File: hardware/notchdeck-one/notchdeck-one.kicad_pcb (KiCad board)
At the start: 4 copper layers, 0 parts

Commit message: Add verified provisional controller PCB floorplan
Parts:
- added C1: 100nF, Capacitor_SMD:C_0402_1005Metric, F.Cu at (92.5, 68.5)
- added C10: 100nF, Capacitor_SMD:C_0402_1005Metric, F.Cu at (61.5, 83.0)
- added C11: 100nF, Capacitor_SMD:C_0402_1005Metric, F.Cu at (75.7, 111.5)
- added C12: 1uF, Capacitor_SMD:C_0402_1005Metric, F.Cu at (75.7, 114.0)
- added C13: 1uF, Capacitor_SMD:C_0805_2012Metric, F.Cu at (119.0, 72.0)
- added C14: 100nF, Capacitor_SMD:C_0402_1005Metric, F.Cu at (66.5, 99.5)
- added C15: 100nF, Capacitor_SMD:C_0402_1005Metric, F.Cu at (66.5, 111.5)
- added C16: 100nF, Capacitor_SMD:C_0402_1005Metric, F.Cu at (66.5, 123.5)
- added C17: 100nF, Capacitor_SMD:C_0402_1005Metric, F.Cu at (66.5, 135.5)
- added C18: 4.7uF, Capacitor_SMD:C_0805_2012Metric, F.Cu at (69.5, 73.0)
- added C19: 4.7uF, Capacitor_SMD:C_0805_2012Metric, F.Cu at (62.5, 74.0)
- added C2: 100nF, Capacitor_SMD:C_0402_1005Metric, F.Cu at (97.2, 68.5)
- added C20: 100nF, Capacitor_SMD:C_0402_1005Metric, F.Cu at (114.0, 71.0)
- added C21: 100nF, Capacitor_SMD:C_0402_1005Metric, F.Cu at (122.0, 73.2)
- added C22: 100nF, Capacitor_SMD:C_0402_1005Metric, F.Cu at (141.0, 73.2)
- added C23: 100nF, Capacitor_SMD:C_0402_1005Metric, F.Cu at (160.0, 73.2)
- added C24: 100nF, Capacitor_SMD:C_0402_1005Metric, F.Cu at (179.0, 73.2)
- added C25: 100nF, Capacitor_SMD:C_0402_1005Metric, F.Cu at (179.0, 92.2)
- added C26: 100nF, Capacitor_SMD:C_0402_1005Metric, F.Cu at (160.0, 92.2)
- added C27: 100nF, Capacitor_SMD:C_0402_1005Metric, F.Cu at (141.0, 92.2)
- added C28: 100nF, Capacitor_SMD:C_0402_1005Metric, F.Cu at (122.0, 92.2)
- added C29: 100nF, Capacitor_SMD:C_0402_1005Metric, F.Cu at (122.0, 111.2)
- added C3: 1uF, Capacitor_SMD:C_0402_1005Metric, F.Cu at (94.8, 68.5)
- added C30: 100nF, Capacitor_SMD:C_0402_1005Metric, F.Cu at (141.0, 111.2)
- added C31: 100nF, Capacitor_SMD:C_0402_1005Metric, F.Cu at (160.0, 111.2)
- added C32: 100nF, Capacitor_SMD:C_0402_1005Metric, F.Cu at (179.0, 111.2)
- added C33: 100nF, Capacitor_SMD:C_0402_1005Metric, F.Cu at (179.0, 130.2)
- added C34: 100nF, Capacitor_SMD:C_0402_1005Metric, F.Cu at (160.0, 130.2)
- added C35: 100nF, Capacitor_SMD:C_0402_1005Metric, F.Cu at (141.0, 130.2)
- added C36: 100nF, Capacitor_SMD:C_0402_1005Metric, F.Cu at (122.0, 130.2)
- added C37: 100nF, Capacitor_SMD:C_0402_1005Metric, F.Cu at (87.0, 143.0)
- added C4: 1uF, Capacitor_SMD:C_0402_1005Metric, F.Cu at (99.5, 68.5)
- added C5: 10uF, Capacitor_SMD:C_0805_2012Metric, F.Cu at (102.0, 68.5)
- added C6: 100nF, Capacitor_SMD:C_0402_1005Metric, F.Cu at (102.0, 65.5)
- added C7: 1uF, Capacitor_SMD:C_0402_1005Metric, F.Cu at (81.0, 73.0)
- added C8: 1uF, Capacitor_SMD:C_0402_1005Metric, F.Cu at (87.0, 73.0)
- added C9: 10uF, Capacitor_SMD:C_0805_2012Metric, F.Cu at (89.5, 74.0)
- added D1: WS2812B, LED_SMD:LED_OPSCO_SK6812_PLCC4_5.0x5.0mm_P3.1mm, F.Cu at (122.0, 77.0)
- added D10: WS2812B, LED_SMD:LED_OPSCO_SK6812_PLCC4_5.0x5.0mm_P3.1mm, F.Cu at (141.0, 115.0)
- added D11: WS2812B, LED_SMD:LED_OPSCO_SK6812_PLCC4_5.0x5.0mm_P3.1mm, F.Cu at (160.0, 115.0)
- added D12: WS2812B, LED_SMD:LED_OPSCO_SK6812_PLCC4_5.0x5.0mm_P3.1mm, F.Cu at (179.0, 115.0)
- added D13: WS2812B, LED_SMD:LED_OPSCO_SK6812_PLCC4_5.0x5.0mm_P3.1mm, F.Cu at (179.0, 134.0)
- added D14: WS2812B, LED_SMD:LED_OPSCO_SK6812_PLCC4_5.0x5.0mm_P3.1mm, F.Cu at (160.0, 134.0)
- added D15: WS2812B, LED_SMD:LED_OPSCO_SK6812_PLCC4_5.0x5.0mm_P3.1mm, F.Cu at (141.0, 134.0)
- added D16: WS2812B, LED_SMD:LED_OPSCO_SK6812_PLCC4_5.0x5.0mm_P3.1mm, F.Cu at (122.0, 134.0)
- added D17: LED, LED_SMD:LED_0603_1608Metric, F.Cu at (73.0, 54.0)
- added D18: LED, LED_SMD:LED_0603_1608Metric, F.Cu at (78.0, 54.0)
- added D19: B5819W, Diode_SMD:D_SOD-123, F.Cu at (77.0, 67.0)
- added D2: WS2812B, LED_SMD:LED_OPSCO_SK6812_PLCC4_5.0x5.0mm_P3.1mm, F.Cu at (141.0, 77.0)
- added D3: WS2812B, LED_SMD:LED_OPSCO_SK6812_PLCC4_5.0x5.0mm_P3.1mm, F.Cu at (160.0, 77.0)
- added D4: WS2812B, LED_SMD:LED_OPSCO_SK6812_PLCC4_5.0x5.0mm_P3.1mm, F.Cu at (179.0, 77.0)
- added D5: WS2812B, LED_SMD:LED_OPSCO_SK6812_PLCC4_5.0x5.0mm_P3.1mm, F.Cu at (179.0, 96.0)
- added D6: WS2812B, LED_SMD:LED_OPSCO_SK6812_PLCC4_5.0x5.0mm_P3.1mm, F.Cu at (160.0, 96.0)
- added D7: WS2812B, LED_SMD:LED_OPSCO_SK6812_PLCC4_5.0x5.0mm_P3.1mm, F.Cu at (141.0, 96.0)
- added D8: WS2812B, LED_SMD:LED_OPSCO_SK6812_PLCC4_5.0x5.0mm_P3.1mm, F.Cu at (122.0, 96.0)
- added D9: WS2812B, LED_SMD:LED_OPSCO_SK6812_PLCC4_5.0x5.0mm_P3.1mm, F.Cu at (122.0, 115.0)
- added H1: M3 provisional, MountingHole:MountingHole_3.2mm_M3, F.Cu at (55.0, 55.0)
- added H2: M3 provisional, MountingHole:MountingHole_3.2mm_M3, F.Cu at (190.0, 55.0)
- added H3: M3 provisional, MountingHole:MountingHole_3.2mm_M3, F.Cu at (190.0, 150.0)
- added H4: M3 provisional, MountingHole:MountingHole_3.2mm_M3, F.Cu at (55.0, 150.0)
- added J1: USB-C, Connector_USB:USB_C_Receptacle_HRO_TYPE-C-31-M-12, F.Cu at (65.0, 54.4)
- added J2: BAT 1S, Connector_JST:JST_PH_S2B-PH-SM4-TB_1x02-1MP_P2.00mm_Horizontal, F.Cu at (55.8, 79.0)
- added J3: SWD, Connector_PinHeader_1.27mm:PinHeader_2x05_P1.27mm_Vertical_SMD, F.Cu at (93.0, 80.0)
- added J4: TC2030_NL, Connector:Tag-Connect_TC2030-IDC-NL_2x03_P1.27mm_Vertical, F.Cu at (104.0, 80.0)
- added J5: CODE S0, Connector_JST:JST_PH_S2B-PH-SM4-TB_1x02-1MP_P2.00mm_Horizontal, F.Cu at (55.8, 99.0)
- added J6: CODE S1, Connector_JST:JST_PH_S2B-PH-SM4-TB_1x02-1MP_P2.00mm_Horizontal, F.Cu at (55.8, 111.0)
- added J7: CODE S2, Connector_JST:JST_PH_S2B-PH-SM4-TB_1x02-1MP_P2.00mm_Horizontal, F.Cu at (55.8, 123.0)
- added J8: CODE S3, Connector_JST:JST_PH_S2B-PH-SM4-TB_1x02-1MP_P2.00mm_Horizontal, F.Cu at (55.8, 135.0)
- added J9: REV F-N-R, Connector_JST:JST_PH_S3B-PH-SM4-TB_1x03-1MP_P2.00mm_Horizontal, F.Cu at (79.0, 149.2)
- added Q1: AO3401A, Package_TO_SOT_SMD:SOT-23, F.Cu at (76.0, 73.0)
- added R1: 5.1k, Resistor_SMD:R_0402_1005Metric, F.Cu at (61.5, 62.2)
- added R10: 4.7k, Resistor_SMD:R_0402_1005Metric, F.Cu at (86.5, 114.0)
- added R11: 330, Resistor_SMD:R_0402_1005Metric, F.Cu at (114.5, 74.0)
- added R12: 1k, Resistor_SMD:R_0402_1005Metric, F.Cu at (73.0, 56.5)
- added R13: 1k, Resistor_SMD:R_0402_1005Metric, F.Cu at (78.0, 56.5)
- added R14: 10k, Resistor_SMD:R_0402_1005Metric, F.Cu at (62.0, 97.2)
- added R15: 10k, Resistor_SMD:R_0402_1005Metric, F.Cu at (62.0, 109.2)
- added R16: 10k, Resistor_SMD:R_0402_1005Metric, F.Cu at (62.0, 121.2)
- added R17: 10k, Resistor_SMD:R_0402_1005Metric, F.Cu at (62.0, 133.2)
- added R18: 1k, Resistor_SMD:R_0402_1005Metric, F.Cu at (64.0, 99.5)
- added R19: 1k, Resistor_SMD:R_0402_1005Metric, F.Cu at (64.0, 111.5)
- added R2: 5.1k, Resistor_SMD:R_0402_1005Metric, F.Cu at (68.5, 62.2)
- added R20: 1k, Resistor_SMD:R_0402_1005Metric, F.Cu at (64.0, 123.5)
- added R21: 1k, Resistor_SMD:R_0402_1005Metric, F.Cu at (64.0, 135.5)
- added R22: 100k, Resistor_SMD:R_0402_1005Metric, F.Cu at (71.5, 66.5)
- added R23: 100k, Resistor_SMD:R_0402_1005Metric, F.Cu at (78.0, 143.0)
- added R24: 100k, Resistor_SMD:R_0402_1005Metric, F.Cu at (80.5, 143.0)
- added R25: 1k, Resistor_SMD:R_0402_1005Metric, F.Cu at (84.0, 143.0)
- added R26: 100k, Resistor_SMD:R_0402_1005Metric, F.Cu at (108.0, 73.0)
- added R3: 2k, Resistor_SMD:R_0402_1005Metric, F.Cu at (69.0, 69.5)
- added R4: 100k, Resistor_SMD:R_0402_1005Metric, F.Cu at (73.0, 73.0)
- added R5: 1k, Resistor_SMD:R_0402_1005Metric, F.Cu at (73.0, 70.5)
- added R6: 4.7k, Resistor_SMD:R_0402_1005Metric, F.Cu at (67.0, 82.0)
- added R7: 4.7k, Resistor_SMD:R_0402_1005Metric, F.Cu at (67.0, 84.0)
- added R8: 100k, Resistor_SMD:R_0402_1005Metric, F.Cu at (67.0, 86.0)
- added R9: 4.7k, Resistor_SMD:R_0402_1005Metric, F.Cu at (86.5, 111.5)
- added SW1: SW_Push, Button_Switch_SMD:SW_Push_1P1T_XKB_TS-1187A, F.Cu at (122.0, 84.0)
- added SW10: SW_Push, Button_Switch_SMD:SW_Push_1P1T_XKB_TS-1187A, F.Cu at (141.0, 122.0)
- added SW11: SW_Push, Button_Switch_SMD:SW_Push_1P1T_XKB_TS-1187A, F.Cu at (160.0, 122.0)
- added SW12: SW_Push, Button_Switch_SMD:SW_Push_1P1T_XKB_TS-1187A, F.Cu at (179.0, 122.0)
- added SW13: SW_Push, Button_Switch_SMD:SW_Push_1P1T_XKB_TS-1187A, F.Cu at (122.0, 141.0)
- added SW14: SW_Push, Button_Switch_SMD:SW_Push_1P1T_XKB_TS-1187A, F.Cu at (141.0, 141.0)
- added SW15: SW_Push, Button_Switch_SMD:SW_Push_1P1T_XKB_TS-1187A, F.Cu at (160.0, 141.0)
- added SW16: SW_Push, Button_Switch_SMD:SW_Push_1P1T_XKB_TS-1187A, F.Cu at (179.0, 141.0)
- added SW17: RESET, Button_Switch_SMD:SW_Push_1P1T_XKB_TS-1187A, F.Cu at (105.5, 61.0)
- added SW2: SW_Push, Button_Switch_SMD:SW_Push_1P1T_XKB_TS-1187A, F.Cu at (141.0, 84.0)
- added SW3: SW_Push, Button_Switch_SMD:SW_Push_1P1T_XKB_TS-1187A, F.Cu at (160.0, 84.0)
- added SW4: SW_Push, Button_Switch_SMD:SW_Push_1P1T_XKB_TS-1187A, F.Cu at (179.0, 84.0)
- added SW5: SW_Push, Button_Switch_SMD:SW_Push_1P1T_XKB_TS-1187A, F.Cu at (122.0, 103.0)
- added SW6: SW_Push, Button_Switch_SMD:SW_Push_1P1T_XKB_TS-1187A, F.Cu at (141.0, 103.0)
- added SW7: SW_Push, Button_Switch_SMD:SW_Push_1P1T_XKB_TS-1187A, F.Cu at (160.0, 103.0)
- added SW8: SW_Push, Button_Switch_SMD:SW_Push_1P1T_XKB_TS-1187A, F.Cu at (179.0, 103.0)
- added SW9: SW_Push, Button_Switch_SMD:SW_Push_1P1T_XKB_TS-1187A, F.Cu at (122.0, 122.0)
- added U1: E73-2G4M08S1C, notchdeck:EBYTE_E73-2G4M08S1C, F.Cu at (93.0, 66.0)
- added U2: AP2112K-3.3, Package_TO_SOT_SMD:SOT-23-5, F.Cu at (84.0, 74.0)
- added U3: MCP73832-2-OT, Package_TO_SOT_SMD:SOT-23-5, F.Cu at (66.0, 72.0)
- added U4: MAX17048, Package_DFN_QFN:TDFN-8-1EP_2x2mm_P0.5mm_EP0.8x1.2mm, F.Cu at (64.0, 83.0)
- added U5: AS5600, Package_SO:SOIC-8_3.9x4.9mm_P1.27mm, F.Cu at (81.0, 113.0)
- added U7: USBLC6-2SC6, Package_TO_SOT_SMD:SOT-23-6, F.Cu at (65.0, 63.8)
- added U8: 74AHCT1G125, Package_TO_SOT_SMD:SOT-23-5, F.Cu at (111.0, 72.0)
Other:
- board outline added: 145 x 105 mm
- board text added: "3V3"
- board text added: "ANTENNA: NO COPPER / METAL"
- board text added: "Align magnet to U5 center"
- board text added: "BAT+ GND"
- board text added: "BTN 1"
- board text added: "BTN 10"
- board text added: "BTN 11"
- board text added: "BTN 12"
- board text added: "BTN 2"
- board text added: "BTN 3"
- board text added: "BTN 4"
- board text added: "BTN 5"
- board text added: "BTN 6"
- board text added: "BTN 7"
- board text added: "BTN 8"
- board text added: "BTN 9"
- board text added: "CHG"
- board text added: "DOWN"
- board text added: "LEFT"
- board text added: "LEVER AXIS"
- board text added: "NOTCHDECK ONE"
- board text added: "PROVISIONAL 145 x 105 mm - MECHANICS TBD"
- board text added: "RESET"
- board text added: "REV B / PLACEMENT STUDY"
- board text added: "REV F / N / R"
- board text added: "RIGHT"
- board text added: "S0"
- board text added: "S1"
- board text added: "S2"
- board text added: "S3"
- board text added: "SWD"
- board text added: "TC2030"
- board text added: "UNROUTED / DO NOT FABRICATE"
- board text added: "UP"
- board text added: "USB"

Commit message: Source controller BOM from JLCPCB and align selected footprints
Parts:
- D1, D10, D11, D12, D13, D14, D15, D16, D2, D3, D4, D5, D6, D7, D8, D9: footprint LED_SMD:LED_OPSCO_SK6812_PLCC4_5.0x5.0mm_P3.1mm -> notchdeck:LED_XINGLIGHT_XL-5050RGBC-2812B
- J3: footprint Connector_PinHeader_1.27mm:PinHeader_2x05_P1.27mm_Vertical_SMD -> notchdeck:Samtec_FTSH-105-01-L-DV-K
- moved J3 2.00 mm to (93.0, 82.0)

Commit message: Support independent magnetic and Gray-coded power and brake handles
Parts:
- added C38: 100nF, Capacitor_SMD:C_0402_1005Metric, F.Cu at (103.0, 100.3)
- added C39: 100nF, Capacitor_SMD:C_0402_1005Metric, F.Cu at (137.0, 65.0)
- added C40: 100nF, Capacitor_SMD:C_0402_1005Metric, F.Cu at (162.0, 65.0)
- added C41: 100nF, Capacitor_SMD:C_0402_1005Metric, F.Cu at (103.0, 113.0)
- added C42: 100nF, Capacitor_SMD:C_0402_1005Metric, F.Cu at (103.0, 120.0)
- added C43: 100nF, Capacitor_SMD:C_0402_1005Metric, F.Cu at (103.0, 127.0)
- added J10: POWER MAG, Connector_JST:JST_PH_S4B-PH-SM4-TB_1x04-1MP_P2.00mm_Horizontal, F.Cu at (133.0, 55.8)
- added J11: BRAKE MAG, Connector_JST:JST_PH_S4B-PH-SM4-TB_1x04-1MP_P2.00mm_Horizontal, F.Cu at (158.0, 55.8)
- added J12: POWER S0, Connector_JST:JST_PH_S2B-PH-SM4-TB_1x02-1MP_P2.00mm_Horizontal, F.Cu at (189.2, 95.0)
- added J13: POWER S1, Connector_JST:JST_PH_S2B-PH-SM4-TB_1x02-1MP_P2.00mm_Horizontal, F.Cu at (189.2, 114.0)
- added J14: POWER S2, Connector_JST:JST_PH_S2B-PH-SM4-TB_1x02-1MP_P2.00mm_Horizontal, F.Cu at (189.2, 133.0)
- added R27: 4.7k, Resistor_SMD:R_0402_1005Metric, F.Cu at (99.0, 103.0)
- added R28: 4.7k, Resistor_SMD:R_0402_1005Metric, F.Cu at (102.0, 103.0)
- added R29: 4.7k, Resistor_SMD:R_0402_1005Metric, F.Cu at (105.0, 103.0)
- added R30: 4.7k, Resistor_SMD:R_0402_1005Metric, F.Cu at (108.0, 103.0)
- added R31: 10k, Resistor_SMD:R_0402_1005Metric, F.Cu at (97.0, 111.0)
- added R32: 10k, Resistor_SMD:R_0402_1005Metric, F.Cu at (97.0, 118.0)
- added R33: 10k, Resistor_SMD:R_0402_1005Metric, F.Cu at (97.0, 125.0)
- added R34: 1k, Resistor_SMD:R_0402_1005Metric, F.Cu at (100.0, 113.0)
- added R35: 1k, Resistor_SMD:R_0402_1005Metric, F.Cu at (100.0, 120.0)
- added R36: 1k, Resistor_SMD:R_0402_1005Metric, F.Cu at (100.0, 127.0)
- added R37: 0, Resistor_SMD:R_0603_1608Metric, F.Cu at (87.0, 111.0)
- added R38: 0, Resistor_SMD:R_0603_1608Metric, F.Cu at (87.0, 114.0)
- added R39: 10k, Resistor_SMD:R_0402_1005Metric, F.Cu at (106.0, 69.0)
- added R40: 10k, Resistor_SMD:R_0402_1005Metric, F.Cu at (98.0, 98.0)
- added R41: 10k, Resistor_SMD:R_0402_1005Metric, F.Cu at (98.0, 100.0)
- added U10: USBLC6-2SC6, Package_TO_SOT_SMD:SOT-23-6, F.Cu at (133.0, 65.0)
- added U11: USBLC6-2SC6, Package_TO_SOT_SMD:SOT-23-6, F.Cu at (158.0, 65.0)
- added U9: TCA9543APWR, Package_SO:TSSOP-14_4.4x5mm_P0.65mm, F.Cu at (103.0, 96.0)
- J5: value CODE S0 -> BRAKE S0
- J6: value CODE S1 -> BRAKE S1
- J7: value CODE S2 -> BRAKE S2
- J8: value CODE S3 -> BRAKE S3
- moved R10 25.7 mm to (98.0, 91.0)
- moved R9 22.6 mm to (96.0, 91.0)
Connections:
- net /MCU/nRESET renamed /nRESET
- U1 pad 10: unconnected-(U1-P0.30/AIN6-Pad10) -> /POWER_S2
- U1 pad 8: unconnected-(U1-P0.29/AIN5-Pad8) -> /POWER_S0
- U1 pad 9: unconnected-(U1-P0.31/AIN7-Pad9) -> /POWER_S1
- U5 pad 6: /I2C0_SDA -> /Lever/U5_POWER_MAG_SDA
- U5 pad 7: /I2C0_SCL -> /Lever/U5_POWER_MAG_SCL
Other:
- board text added: "BRAKE MAG"
- board text added: "BRAKE S0"
- board text added: "BRAKE S1"
- board text added: "BRAKE S2"
- board text added: "BRAKE S3"
- board text added: "J10 EXT: REMOVE R37 + R38"
- board text added: "POWER / COMBINED AXIS"
- board text added: "POWER MAG"
- board text added: "PWR S0"
- board text added: "PWR S1"
- board text added: "PWR S2"
- board text added: "REV C / DUAL HANDLES"
- board text removed: "LEVER AXIS"
- board text removed: "REV B / PLACEMENT STUDY"
- board text removed: "S0"
- board text removed: "S1"
- board text removed: "S2"
- board text removed: "S3"

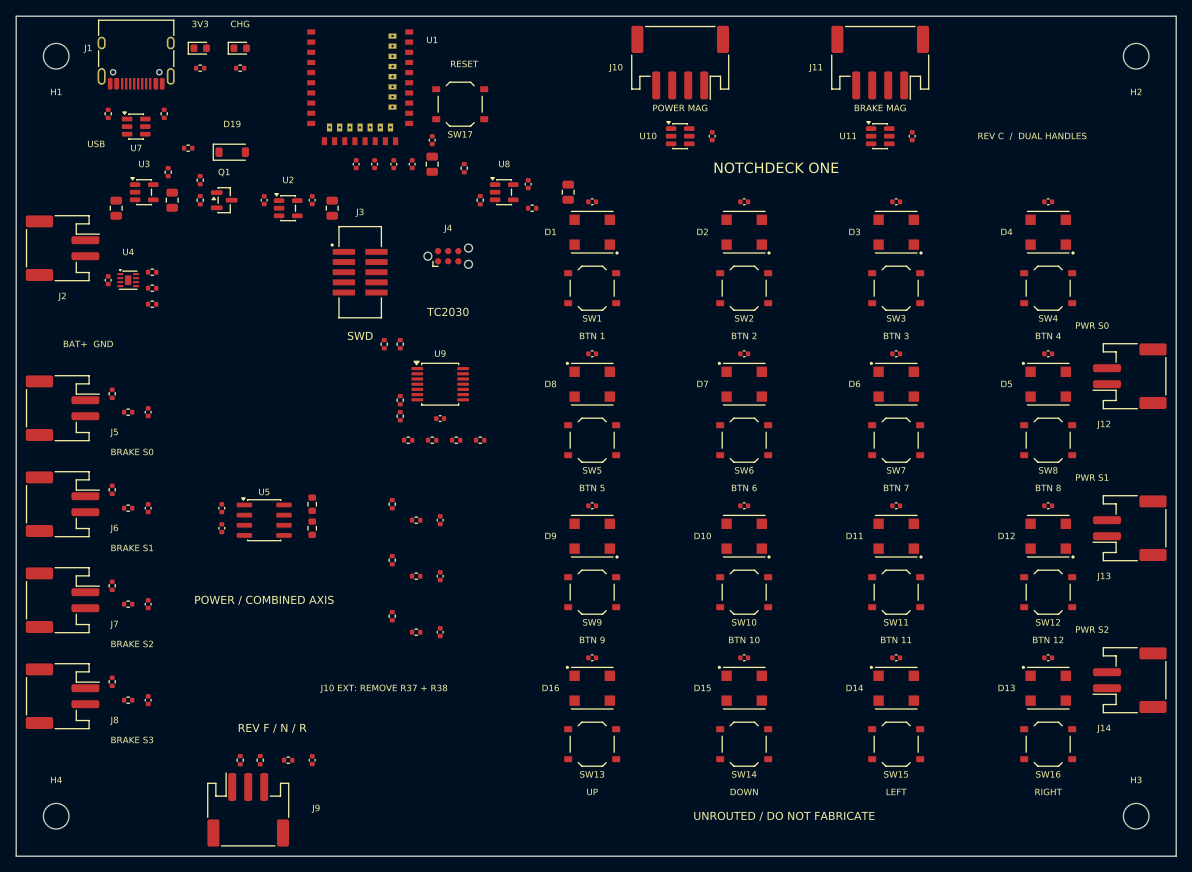
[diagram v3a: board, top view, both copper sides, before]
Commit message: Add keyed harnesses and build plan for Japanese-style dual and mascon handles
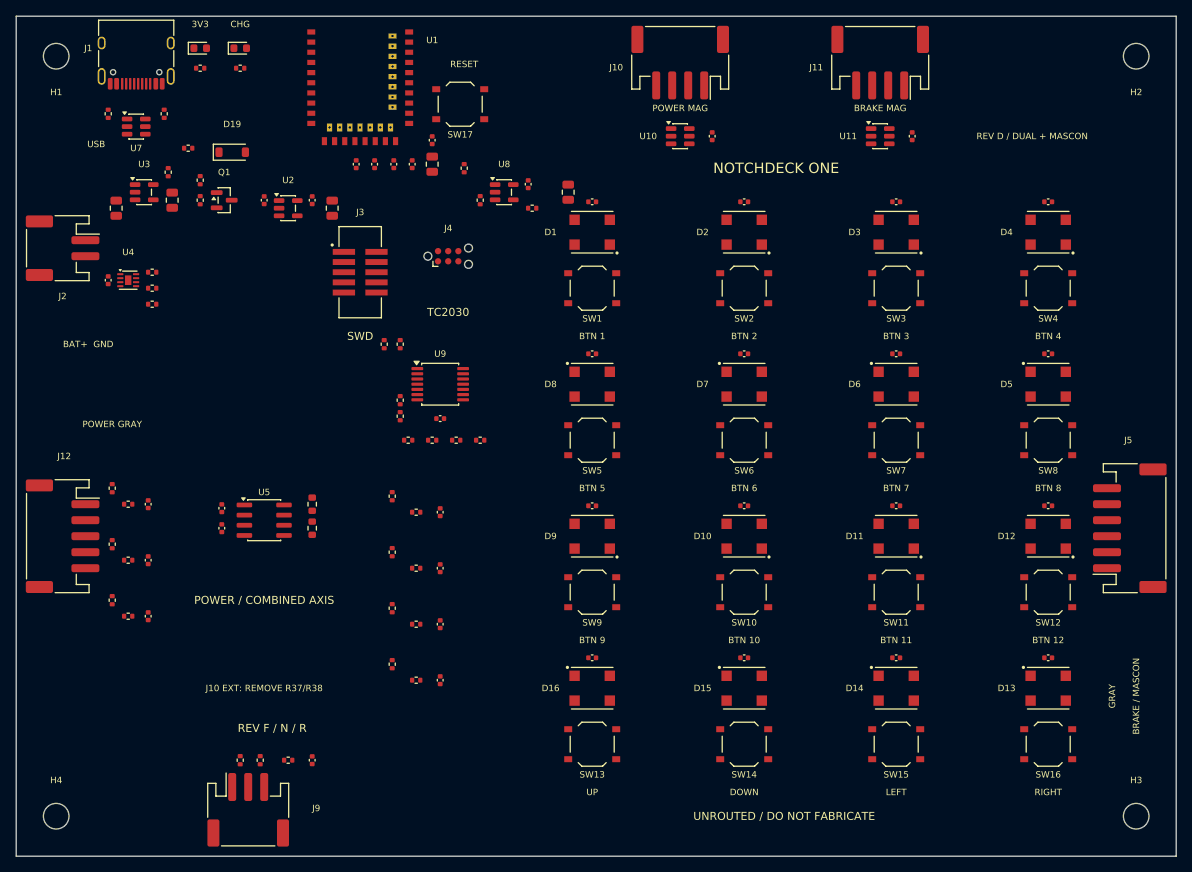
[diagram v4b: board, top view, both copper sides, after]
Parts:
- removed J13: POWER S1, Connector_JST:JST_PH_S2B-PH-SM4-TB_1x02-1MP_P2.00mm_Horizontal
- removed J14: POWER S2, Connector_JST:JST_PH_S2B-PH-SM4-TB_1x02-1MP_P2.00mm_Horizontal
- removed J6: BRAKE S1, Connector_JST:JST_PH_S2B-PH-SM4-TB_1x02-1MP_P2.00mm_Horizontal
- removed J7: BRAKE S2, Connector_JST:JST_PH_S2B-PH-SM4-TB_1x02-1MP_P2.00mm_Horizontal
- removed J8: BRAKE S3, Connector_JST:JST_PH_S2B-PH-SM4-TB_1x02-1MP_P2.00mm_Horizontal
- J12: value POWER S0 -> POWER GRAY; footprint Connector_JST:JST_PH_S2B-PH-SM4-TB_1x02-1MP_P2.00mm_Horizontal -> Connector_JST:JST_PH_S5B-PH-SM4-TB_1x05-1MP_P2.00mm_Horizontal
- J5: value BRAKE S0 -> BRAKE / MASCON GRAY; footprint Connector_JST:JST_PH_S2B-PH-SM4-TB_1x02-1MP_P2.00mm_Horizontal -> Connector_JST:JST_PH_S6B-PH-SM4-TB_1x06-1MP_P2.00mm_Horizontal
- moved J12 134.9 mm to (55.8, 115.0), turned to -90 degrees
- moved J5 134.2 mm to (189.2, 114.0), turned to 90 degrees
- moved C14 38.6 mm to (103.0, 112.0)
- moved R18 38.1 mm to (100.0, 112.0)
- moved R14 37.3 mm to (97.0, 110.0)
- moved C15 37.3 mm to (103.0, 119.0)
- moved R19 36.8 mm to (100.0, 119.0)
- moved C16 36.6 mm to (103.0, 126.0)
- moved C17 36.6 mm to (103.0, 133.0)
- moved C41 36.6 mm to (66.5, 111.0)
- moved C42 36.6 mm to (66.5, 118.0)
- moved C43 36.6 mm to (66.5, 125.0)
- moved R20 36.1 mm to (100.0, 126.0)
- moved R21 36.1 mm to (100.0, 133.0)
- moved R34 36.1 mm to (64.0, 111.0)
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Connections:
- J12 pad 1: Net-(J12-Pin_1) -> GND
- J12 pad 2: GND -> /Lever/POWER_RAW_S0
- J5 pad 1: Net-(J5-Pin_1) -> GND
- J5 pad 2: GND -> /Lever/BRAKE_RAW_S0
- R14 pad 2: Net-(J5-Pin_1) -> /Lever/BRAKE_RAW_S0
- R15 pad 2: Net-(J6-Pin_1) -> /Lever/BRAKE_RAW_S1
- R16 pad 2: Net-(J7-Pin_1) -> /Lever/BRAKE_RAW_S2
- R17 pad 2: Net-(J8-Pin_1) -> /Lever/BRAKE_RAW_S3
- R18 pad 1: Net-(J5-Pin_1) -> /Lever/BRAKE_RAW_S0
- R19 pad 1: Net-(J6-Pin_1) -> /Lever/BRAKE_RAW_S1
- R20 pad 1: Net-(J7-Pin_1) -> /Lever/BRAKE_RAW_S2
- R21 pad 1: Net-(J8-Pin_1) -> /Lever/BRAKE_RAW_S3
- R31 pad 2: Net-(J12-Pin_1) -> /Lever/POWER_RAW_S0
- R32 pad 2: Net-(J13-Pin_1) -> /Lever/POWER_RAW_S1
- R33 pad 2: Net-(J14-Pin_1) -> /Lever/POWER_RAW_S2
- R34 pad 1: Net-(J12-Pin_1) -> /Lever/POWER_RAW_S0
- R35 pad 1: Net-(J13-Pin_1) -> /Lever/POWER_RAW_S1
- R36 pad 1: Net-(J14-Pin_1) -> /Lever/POWER_RAW_S2
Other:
- board text added: "BRAKE / MASCON"
- board text added: "GRAY"
- board text added: "GRAY CONTACTS: LEAVE 3V3 WIRE OUT"
- board text added: "J10 EXT: REMOVE R37/R38"
- board text added: "J12 POWER: 1 GND / 2 S0 / 3 S1 / 4 S2 / 5 3V3"
- board text added: "J5 BRAKE / MASCON: 1 GND / 2 S0 / 3 S1 / 4 S2 / 5 S3 / 6 3V3"
- board text added: "POWER GRAY"
- board text added: "REV D / DUAL + MASCON"
- board text removed: "BRAKE S0"
- board text removed: "BRAKE S1"
- board text removed: "BRAKE S2"
- board text removed: "BRAKE S3"
- board text removed: "J10 EXT: REMOVE R37 + R38"
- board text removed: "PWR S0"
- board text removed: "PWR S1"
- board text removed: "PWR S2"
- board text removed: "REV C / DUAL HANDLES"
